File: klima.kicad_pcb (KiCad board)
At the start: 2 copper layers, 70 x 30 mm, 16 parts, among them J101 ESP8266-01S, J102 PROG, J103 PWR, J104 serial, J105 PWR, SW101 BOOT, U101 WPMDH1100xx1S, U102 DHT11

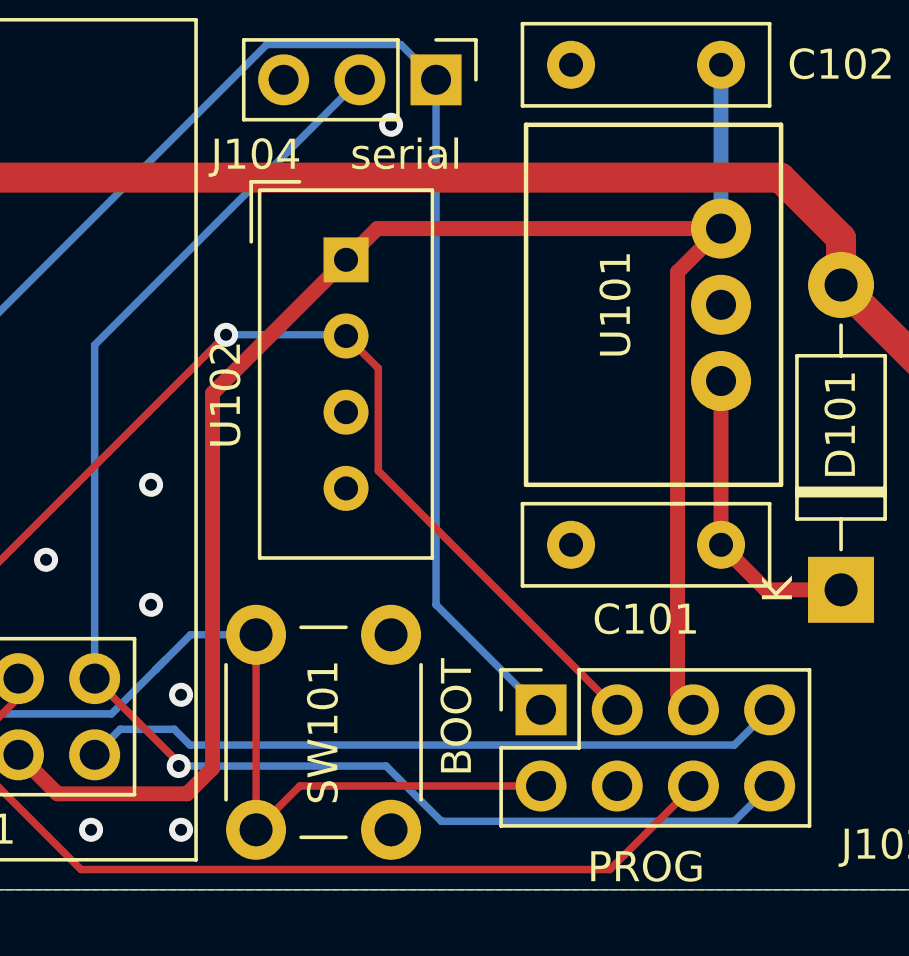
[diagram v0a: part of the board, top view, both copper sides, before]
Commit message: Add  missing pullup
The DHT sensor has an open collector output and need a pullup.
Add the missing pullup.

Signed-off-by: Benedikt Spranger <b.spranger@linutronix.de>
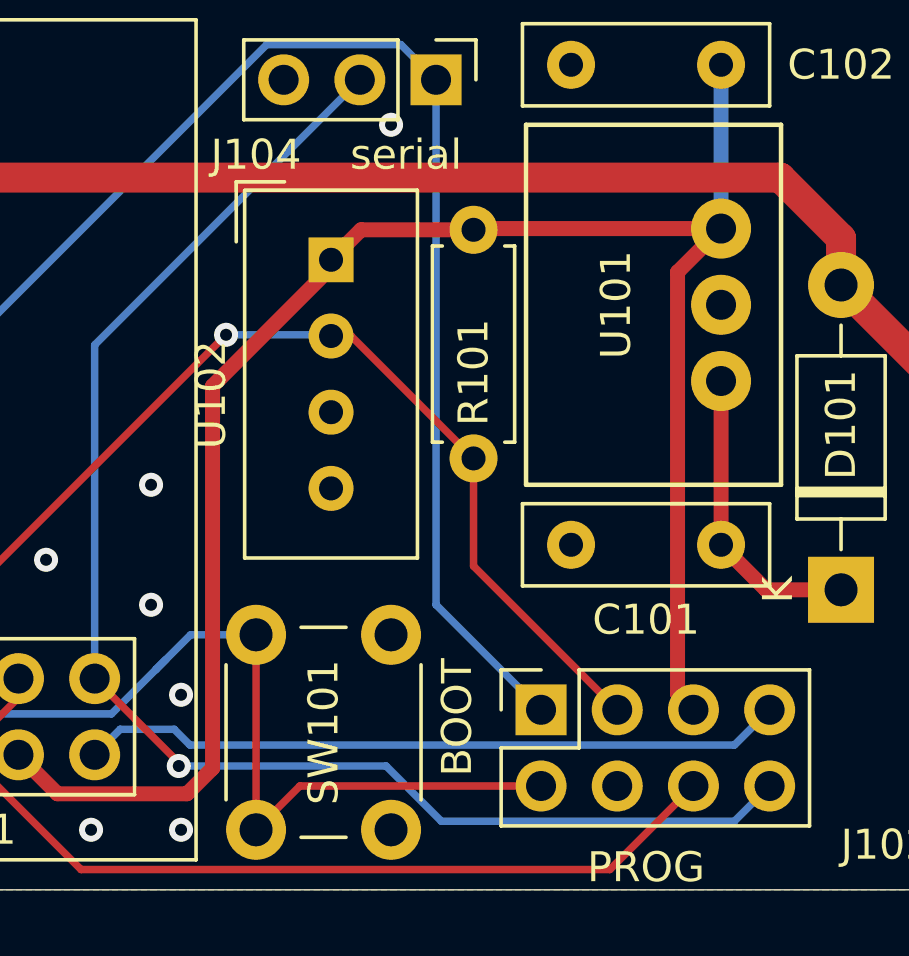
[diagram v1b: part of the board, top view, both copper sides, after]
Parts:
- added R101: 10k, Resistor_THT:R_Axial_DIN0207_L6.3mm_D2.5mm_P7.62mm_Horizontal, F.Cu at (140.2, 78.0)
- moved U102 0.50 mm to (135.5, 79.0)
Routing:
- net +3V3: track 61.4 -> 62.5 mm
- net /IO2: track 38.1 -> 38.7 mm

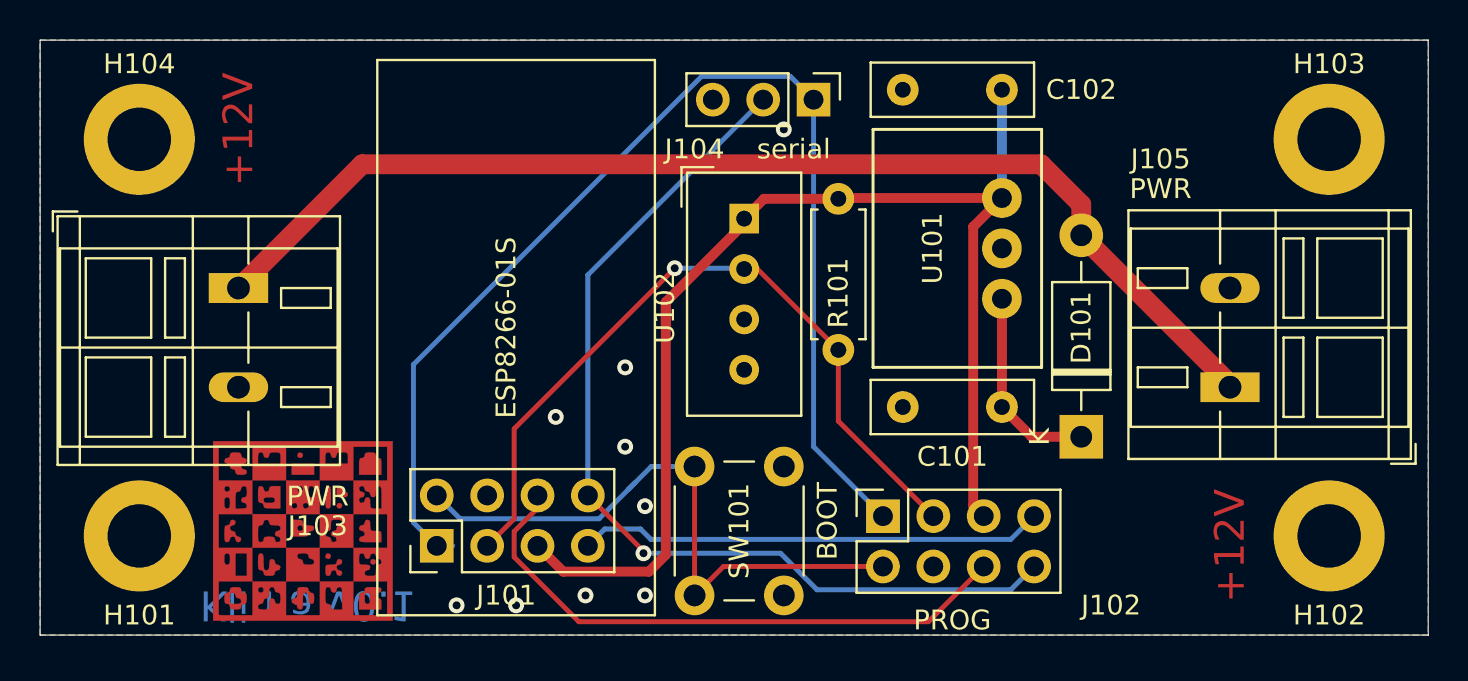
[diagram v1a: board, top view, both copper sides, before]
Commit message: Rework ESP-01S connectors
The ESP-01S schematic use a different numbering scheme for pinheaders.
Revisit the schematic and consolidate schematic and footprint
numbering scheme.

Signed-off-by: Benedikt Spranger <b.spranger@linutronix.de>
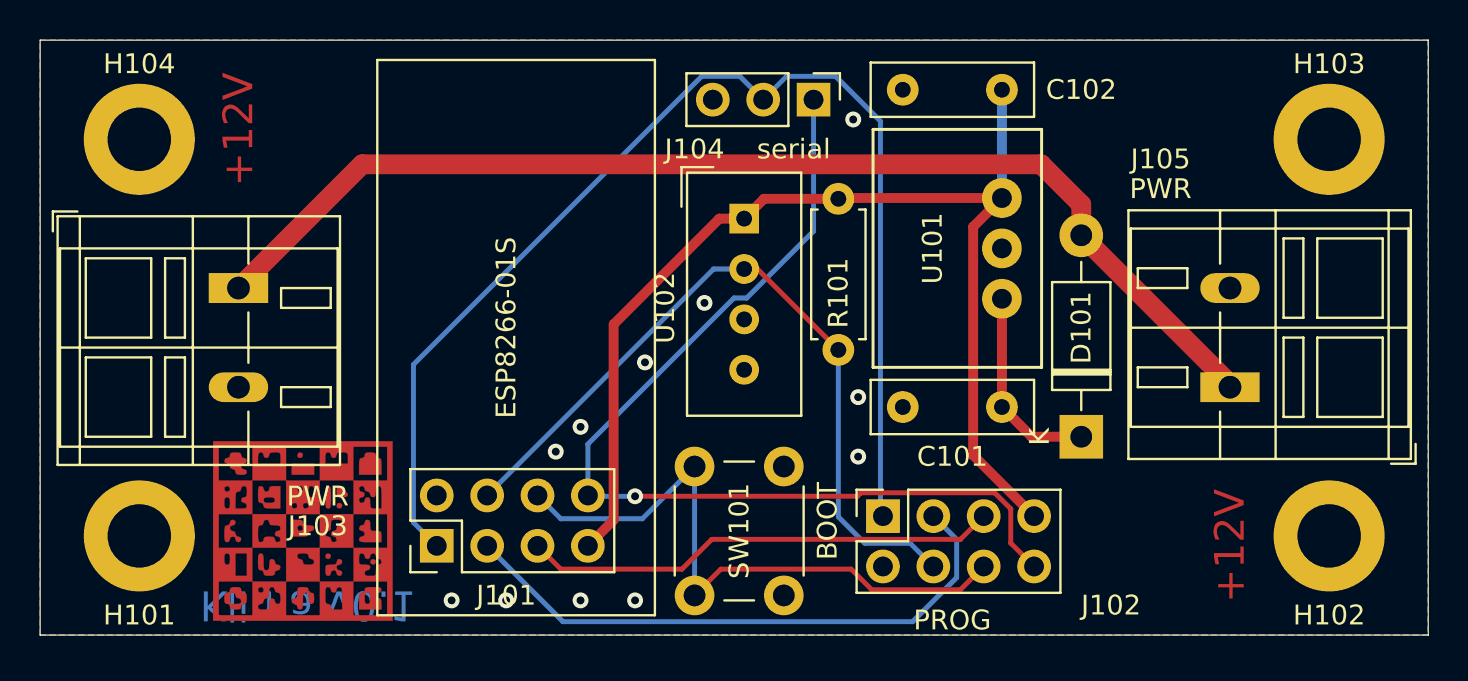
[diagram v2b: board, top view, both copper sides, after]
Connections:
- J101 pad 1: /RX -> /TX
- J101 pad 2: /IO0 -> GND
- J101 pad 3: /IO2 -> /EN
- J101 pad 4: GND -> /IO2
- J101 pad 5: +3V3 -> /~RST
- J101 pad 6: /~RST -> /IO0
- J101 pad 7: /EN -> +3V3
- J101 pad 8: /TX -> /RX
- J102 pad 1: /RX -> /TX
- J102 pad 2: /IO0 -> GND
- J102 pad 3: /IO2 -> /EN
- J102 pad 4: GND -> /IO2
- J102 pad 5: +3V3 -> /~RST
- J102 pad 6: /~RST -> /IO0
- J102 pad 7: /EN -> +3V3
- J102 pad 8: /TX -> /RX
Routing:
- net /TX: track 48.6 -> 61.1 mm, vias 1 -> 0
- net /RX: track 59.6 -> 50.2 mm, vias 0 -> 1
- net /EN: track 23.8 -> 29.8 mm
- net /~RST: track 29.8 -> 24.1 mm
- net +3V3: track 62.5 -> 57.8 mm
- net /IO0: track 31.7 -> 32.7 mm
- net /IO2: track 38.7 -> 38.4 mm, vias 1 -> 0
- net GND: vias 9 -> 11
